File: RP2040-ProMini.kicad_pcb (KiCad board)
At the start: 4 copper layers, 17.8 x 33 mm, 41 parts, among them J1 CONN_L, J2 CONN_U, J3 CONN_R2, J4 CONN_R, J5 CONN_R3, Q1 AO3400A, U1 W25Q128JVS, U2 RP2040, U3 TPS63060, U4 W25Q128JVEIQ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

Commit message: Removed drawings on the back side
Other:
- board text removed: "B-B"
- board text removed: "BOOT"
- board text removed: "FLASH"
- board text removed: "MCU"
- board text removed: "QRZ"
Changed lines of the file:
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@@
       ))
   )
-  (gr_line (start 139.446 101.6) (end 139.446 104.14)
-    (stroke (width 0.15) (type default)) (layer "B.SilkS"))
-  (gr_line (start 145.415 120.015) (end 148.59 116.84)
-    (stroke (width 0.15) (type default)) (layer "B.SilkS"))
-  (gr_line (start 137.922 101.6) (end 137.922 104.14)
-    (stroke (width 0.15) (type default)) (layer "B.SilkS"))
-  (gr_line (start 139.7 105.41) (end 139.7 110.49)
-    (stroke (width 0.15) (type default)) (layer "B.SilkS"))
-  (gr_line (start 138.43 116.84) (end 141.605 120.015)
-    (stroke (width 0.15) (type default)) (layer "B.SilkS"))
-  (gr_line (start 148.59 116.84) (end 145.415 113.665)
-    (stroke (width 0.15) (type default)) (layer "B.SilkS"))
-  (gr_line (start 146.304 97.282) (end 143.256 97.282)
-    (stroke (width 0.15) (type default)) (layer "B.SilkS"))
-  (gr_line (start 137.795 125.73) (end 140.716 125.73)
-    (stroke (width 0.15) (type default)) (layer "B.SilkS"))
-  (gr_line (start 146.304 97.282) (end 146.304 100.838)
-    (stroke (width 0.15) (type default)) (layer "B.SilkS"))
-  (gr_line (start 140.716 123.19) (end 137.795 123.19)
-    (stroke (width 0.15) (type default)) (layer "B.SilkS"))
-  (gr_line (start 139.7 110.49) (end 141.605 110.49)
-    (stroke (width 0.15) (type default)) (layer "B.SilkS"))
-  (gr_line (start 137.795 123.19) (end 137.795 125.73)
-    (stroke (width 0.15) (type default)) (layer "B.SilkS"))
-  (gr_line (start 141.605 105.41) (end 139.7 105.41)
-    (stroke (width 0.15) (type default)) (layer "B.SilkS"))
-  (gr_line (start 143.256 100.838) (end 143.256 97.282)
-    (stroke (width 0.15) (type default)) (layer "B.SilkS"))
-  (gr_line (start 138.43 116.84) (end 141.605 113.665)
-    (stroke (width 0.15) (type default)) (layer "B.SilkS"))
-  (gr_line (start 146.304 100.838) (end 144.78 100.838)
-    (stroke (width 0.15) (type default)) (layer "B.SilkS"))
   (gr_circle (center 138.684 103.124) (end 138.43 102.87)
     (stroke (width 0.15) (type default)) (fill none) (layer "F.SilkS"))
@@
     (effects (font (size 0.75 0.75) (thickness 0.15) bold) (justify mirror))
   )
-  (gr_text "FLASH" (at 140.97 107.95 90) (layer "B.SilkS")
-    (effects (font (size 0.75 0.75) (thickness 0.15) bold) (justify mirror))
-  )
   (gr_text "UD-" (at 137.16 96.52 180) (layer "B.SilkS")
     (effects (font (size 0.75 0.75) (thickness 0.15) bold) (justify mirror))
@@
   )
   (gr_text "D20" (at 146.05 124.46) (layer "B.SilkS")
-    (effects (font (size 0.75 0.75) (thickness 0.15) bold) (justify mirror))
-  )
-  (gr_text "MCU" (at 140.97 116.84 90) (layer "B.SilkS")
     (effects (font (size 0.75 0.75) (thickness 0.15) bold) (justify mirror))
   )
@@
     (effects (font (size 0.75 0.75) (thickness 0.15) bold) (justify mirror))
   )
-  (gr_text "B-B" (at 144.78 99.06 90) (layer "B.SilkS")
-    (effects (font (size 0.75 0.75) (thickness 0.15) bold) (justify mirror))
-  )
   (gr_text "D3" (at 137.16 110.49 270) (layer "B.SilkS")
     (effects (font (size 0.75 0.75) (thickness 0.15) bold) (justify mirror))
   )
   (gr_text "D19" (at 147.32 106.68 90) (layer "B.SilkS")
-    (effects (font (size 0.75 0.75) (thickness 0.15) bold) (justify mirror))
-  )
-  (gr_text "BOOT" (at 138.684 102.87 90) (layer "B.SilkS")
     (effects (font (size 0.75 0.75) (thickness 0.15) bold) (justify mirror))
   )
@@
     (effects (font (size 0.75 0.75) (thickness 0.15) bold) (justify mirror))
   )
-  (gr_text "QRZ" (at 139.7 124.46 90) (layer "B.SilkS")
-    (effects (font (size 0.75 0.75) (thickness 0.15) bold) (justify mirror))
-  )

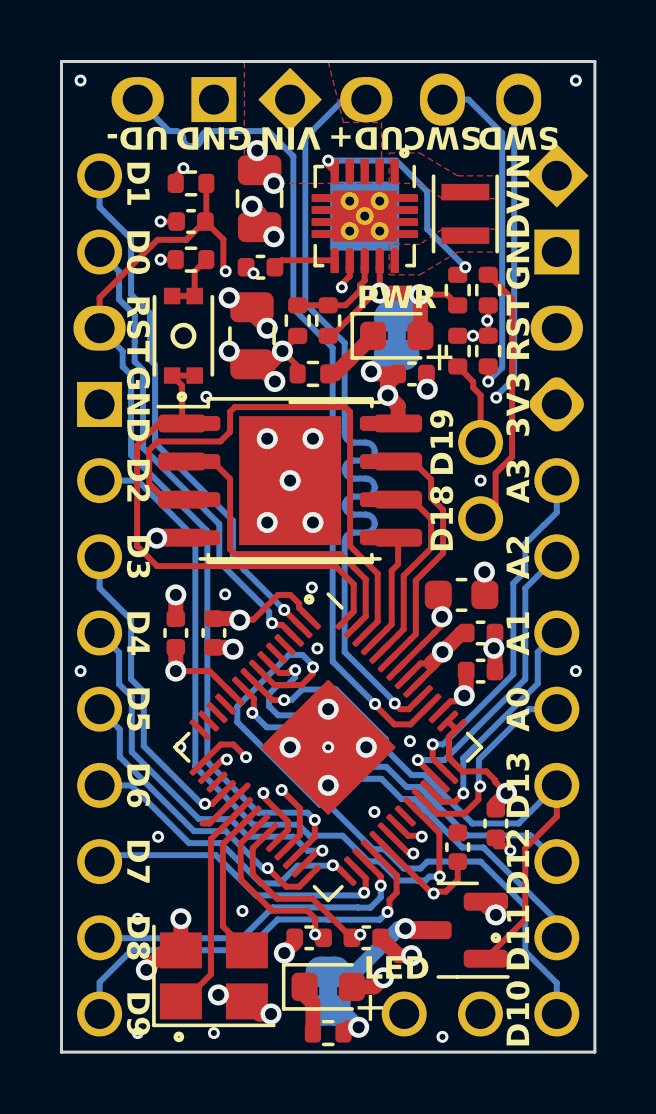
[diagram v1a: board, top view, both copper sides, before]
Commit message: Moved few traces and texts around.
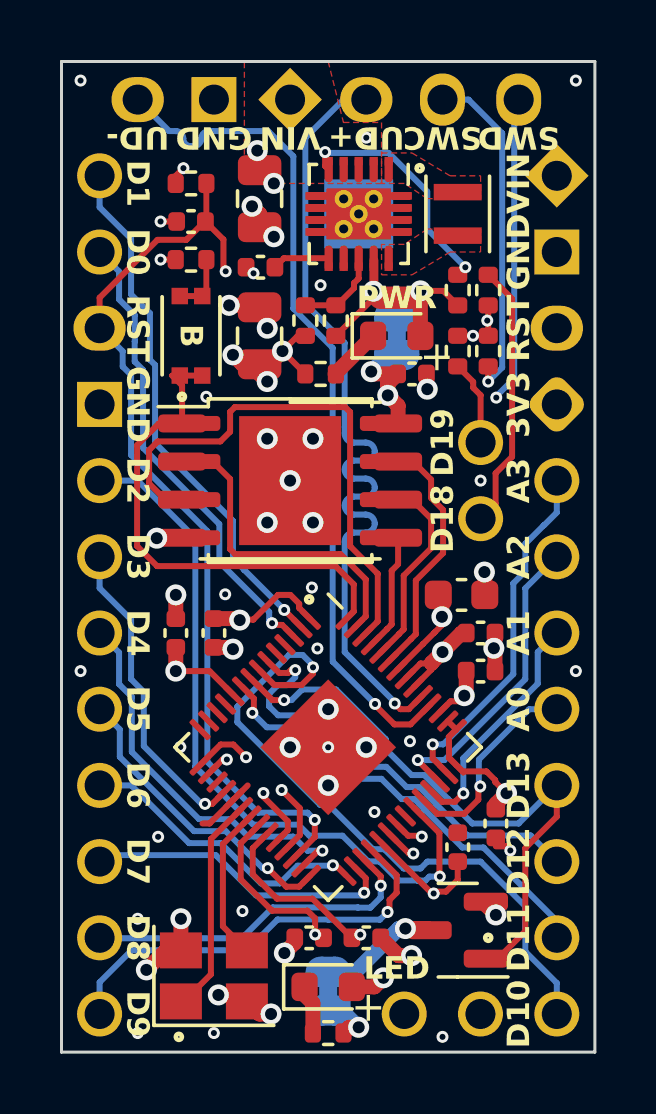
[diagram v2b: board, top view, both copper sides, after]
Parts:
- moved R9 0.25 mm to (143.8, 102.6)
- moved C14 0.25 mm to (141.2, 103.1)
- moved L1 0.25 mm to (147.8, 99.1)
- moved R10 0.25 mm to (142.7, 102.6)
- moved R6 0.25 mm to (143.3, 104.4)
- moved S1 0.25 mm to (138.9, 103.1)
- moved U3 0.21 mm to (144.5, 99.1)
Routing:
- net GND: track 23.4 -> 22.2 mm
- net /VOUT: track 9.63 -> 10.2 mm
- net VIN: vias 2 -> 3
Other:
- board text added: "B"

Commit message: Changed pin number texts, removed D letter
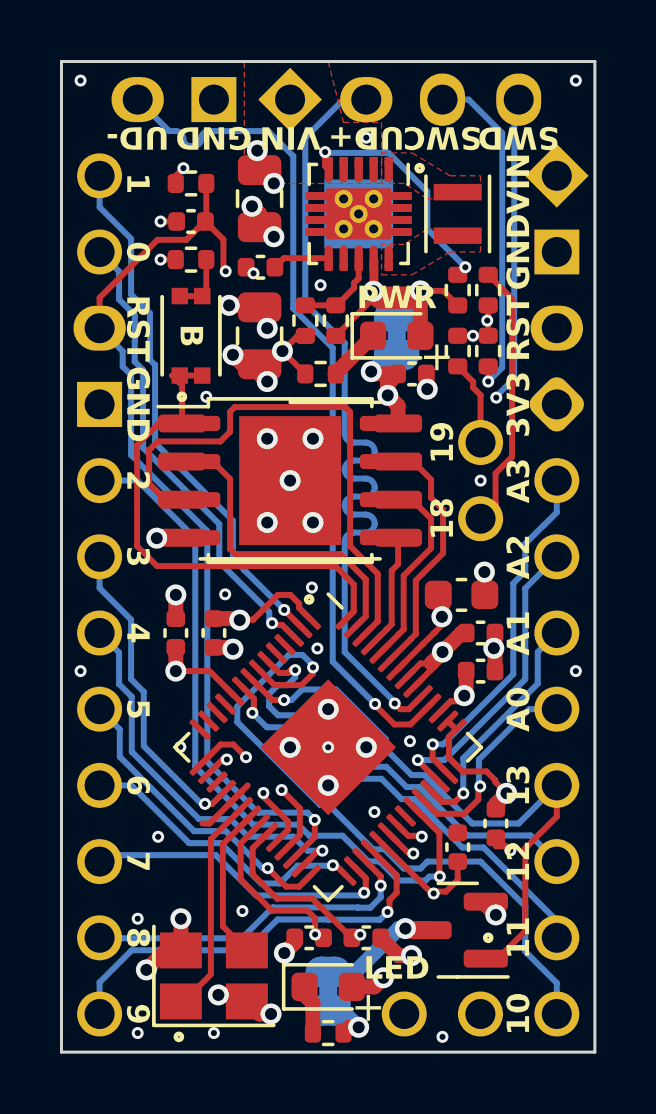
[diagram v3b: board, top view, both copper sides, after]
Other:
- board text added: "0"
- board text added: "1"
- board text added: "10"
- board text added: "11"
- board text added: "12"
- board text added: "13"
- board text added: "14"
- board text added: "15"
- board text added: "16"
- board text added: "17"
- board text added: "18"
- board text added: "19"
- board text added: "2"
- board text added: "20"
- board text added: "21"
- board text added: "3"
- board text added: "4"
- board text added: "5"
- board text added: "6"
- board text added: "7"
- board text added: "8"
- board text added: "9"
- board text removed: "D0"
- board text removed: "D1"
- board text removed: "D10"
- board text removed: "D11"
- board text removed: "D12"
- board text removed: "D13"
- board text removed: "D14"
- board text removed: "D15"
- board text removed: "D16"
- board text removed: "D17"
- board text removed: "D18"
- board text removed: "D19"
- board text removed: "D2"
- board text removed: "D20"
- board text removed: "D21"
- board text removed: "D3"
- board text removed: "D4"
- board text removed: "D5"
- board text removed: "D6"
- board text removed: "D7"
- board text removed: "D8"
- board text removed: "D9"

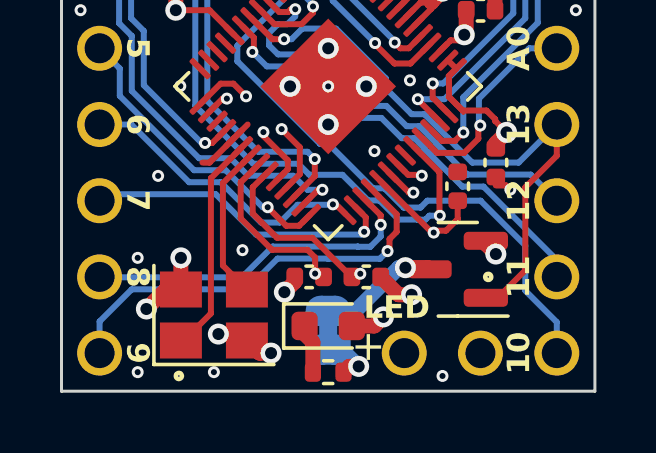
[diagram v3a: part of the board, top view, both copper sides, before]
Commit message: Rotated quartz for better silk markings alignment
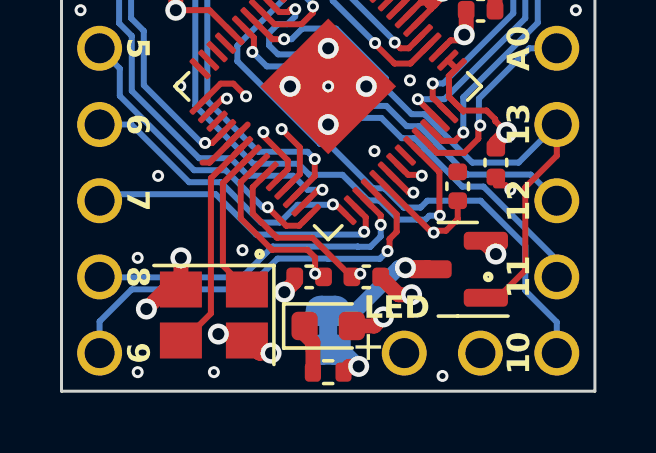
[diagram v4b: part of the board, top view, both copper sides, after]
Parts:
- turned Y1 to 180 degrees
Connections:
- Y1 pad 1: XIN -> XOUT
- Y1 pad 3: XOUT -> XIN
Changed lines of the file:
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@@
   )
   (footprint "Crystal:Crystal_SMD_3225-4Pin_3.2x2.5mm" (layer "F.Cu")
-    (at 139.7 124.46)
+    (at 139.7 124.46 180)
     (descr "SMD Crystal SERIES SMD3225/4 http://www.txccrystal.com/images/pdf/7m-accuracy.pdf, 3.2x2.5mm^2 package")
     (tags "SMD SMT crystal")
@@
     (fp_line (start 1.6 1.25) (end 1.6 -1.25)
       (stroke (width 0.1) (type solid)) (layer "F.Fab"))
-    (pad "1" smd rect (at -1.1 0.85) (size 1.4 1.2) (layers "F.Cu" "F.Paste" "F.Mask")
-      (net 30 "XIN") (pinfunction "1") (pintype "passive"))
-    (pad "2" smd rect (at 1.1 0.85) (size 1.4 1.2) (layers "F.Cu" "F.Paste" "F.Mask")
+    (pad "1" smd rect (at -1.1 0.85 180) (size 1.4 1.2) (layers "F.Cu" "F.Paste" "F.Mask")
+      (net 31 "XOUT") (pinfunction "1") (pintype "passive"))
+    (pad "2" smd rect (at 1.1 0.85 180) (size 1.4 1.2) (layers "F.Cu" "F.Paste" "F.Mask")
       (net 18 "GND") (pinfunction "2") (pintype "passive"))
-    (pad "3" smd rect (at 1.1 -0.85) (size 1.4 1.2) (layers "F.Cu" "F.Paste" "F.Mask")
-      (net 31 "XOUT") (pinfunction "3") (pintype "passive"))
-    (pad "4" smd rect (at -1.1 -0.85) (size 1.4 1.2) (layers "F.Cu" "F.Paste" "F.Mask")
+    (pad "3" smd rect (at 1.1 -0.85 180) (size 1.4 1.2) (layers "F.Cu" "F.Paste" "F.Mask")
+      (net 30 "XIN") (pinfunction "3") (pintype "passive"))
+    (pad "4" smd rect (at -1.1 -0.85 180) (size 1.4 1.2) (layers "F.Cu" "F.Paste" "F.Mask")
       (net 18 "GND") (pinfunction "4") (pintype "passive"))
     (model "${KICAD6_3DMODEL_DIR}/Crystal.3dshapes/Crystal_SMD_3225-4Pin_3.2x2.5mm.wrl"
@@
       ))
   )
-  (gr_circle (center 138.5316 126.492) (end 138.43 126.492)
+  (gr_circle (center 141.224 122.428) (end 141.1224 122.428)
     (stroke (width 0.15) (type default)) (fill none) (layer "F.SilkS"))
   (gr_circle (center 146.558 97.536) (end 146.6596 97.536)

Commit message: Moved few stuff around
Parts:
- moved R4 0.51 mm to (148.8, 102.1)
- moved R8 0.51 mm to (147.8, 102.1)
- moved R2 0.51 mm to (148.8, 104.1)
- moved R3 0.51 mm to (147.8, 104.1)
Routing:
- net Net-(U3-PG): track 7.99 -> 8.57 mm
- net D18_SDA: track 24.7 -> 24.2 mm

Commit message: Moved few stuff around
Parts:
- moved C6 0.76 mm to (149.1, 120.1)
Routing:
- net +3V3: track 36.8 -> 37.3 mm
- net GND: track 22.2 -> 22.3 mm, vias 51 -> 54
